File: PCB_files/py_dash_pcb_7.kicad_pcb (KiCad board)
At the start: 4 copper layers, 203.8 x 102.3 mm, 120 parts, among them J1 Micro_SD_Card_Det1, J2 FFC2B28-40-G, J3 USB_C_Receptacle_USB2.0_14P, J4 CANbus, Q1 DMG2307, Q2 DMG2307, Q3 DMG2307, SW1 nBoot, SW2 SW_Push, SW3 SW_Push, SW4 SW_Push, SW5 SW_Push, SW6 SW_Push, SW7 SW_Push, U1 CM4102008, U2 AP64501SP-13, U3 BD33FC0FP, U4 EMIF06-MSD02N16, U5 TPD8S009DSMR, U6 TPD8S009DSMR, U7 TPD2EUSB30, U8 MCP2515-xST, U9 SN65HVD234, Y1 16Mhz

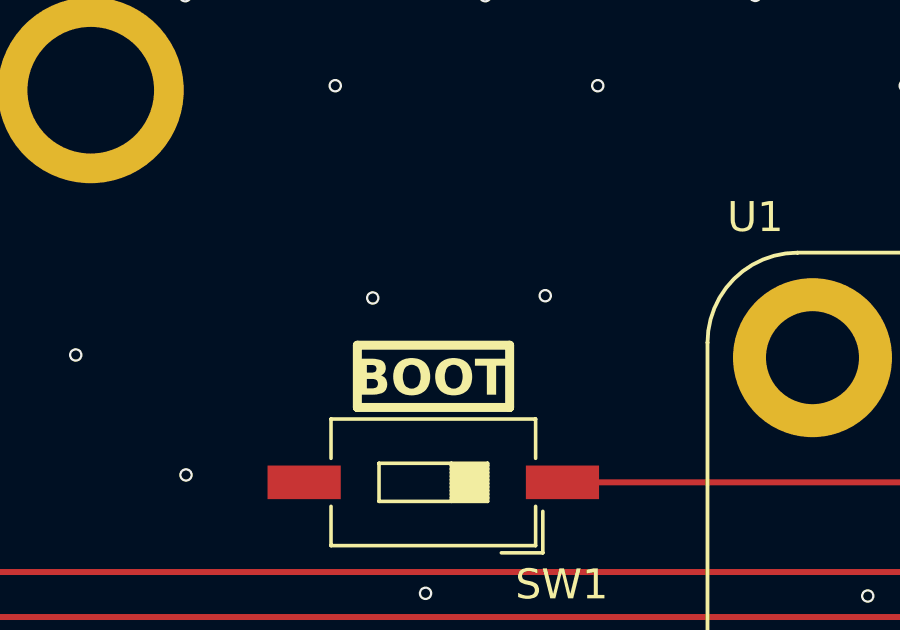
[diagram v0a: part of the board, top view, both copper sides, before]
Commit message: testing updates
D2, D3 part update, PROG direction on boot switch, removed ribbon cable. updated BOM to reflect changes, re-generated gerbers for slight tweaks
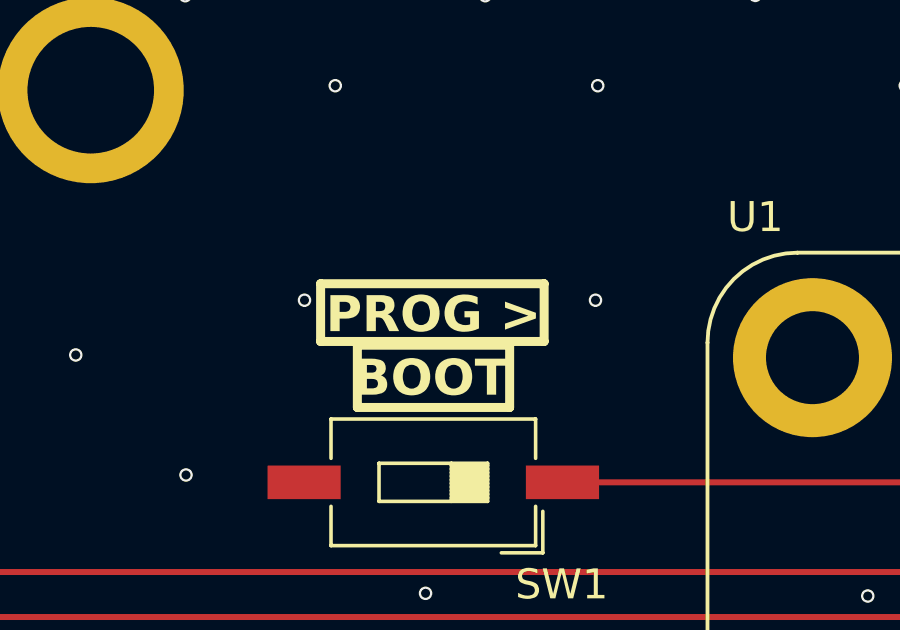
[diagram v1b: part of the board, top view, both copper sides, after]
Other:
- board text added: "PROG >"
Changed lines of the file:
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@@
 		(layer "F.SilkS")
 	)
+	(gr_rect
+		(start 112.5119 56.6)
+		(end 119.9631 58.5252)
+		(stroke
+			(width 0.3)
+			(type solid)
+		)
+		(fill no)
+		(layer "F.SilkS")
+	)
 	(gr_circle
 		(center 131.6855 138.919)
@@
 		(layer "User.2")
 	)
+	(gr_text "PROG >"
+		(at 116.275 57.625 0)
+		(layer "F.SilkS" knockout)
+		(effects
+			(font
+				(size 1.2 1.2)
+				(thickness 0.3)
+				(bold yes)
+			)
+		)
+	)
 	(gr_text "PyDash - LRC\nBatch: B/N 03092025\nRev 2a  03/09/2025"
 		(at 193.475 131.475 0)
@@
 	)
 	(via
-		(at 120 57)
+		(at 121.675 57.15)
 		(size 0.45)
 		(drill 0.3)
@@
 	)
 	(via
-		(at 114.25 57.075)
+		(at 111.975 57.15)
 		(size 0.45)
 		(drill 0.3)
@@
 	)
 	(group ""
-		(members "3c9b0722-073a-432e-a3d1-d2c81758c07c" "63b57dbe-b6a0-4df5-aa83-f81a60a490c0"
+		(members "19b78979-5ce5-45b2-bebb-19f248b3861a" "3c9b0722-073a-432e-a3d1-d2c81758c07c"
+			"63b57dbe-b6a0-4df5-aa83-f81a60a490c0" "6f852d5a-35da-4d5d-9b6d-6f6f37bcda31"
 			"f980980c-96b6-4e08-a395-3558102de11a"
 		)
